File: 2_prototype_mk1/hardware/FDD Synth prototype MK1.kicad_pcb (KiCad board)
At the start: 2 copper layers, 90.2 x 59.7 mm, 21 parts, among them J1 Micro_SD_Card, J2 Conn_02x17_Odd_Even, J3 Conn_01x04_Pin, J4 Conn_01x04_Pin, U1 74AHCT245, U5 MAX98357A

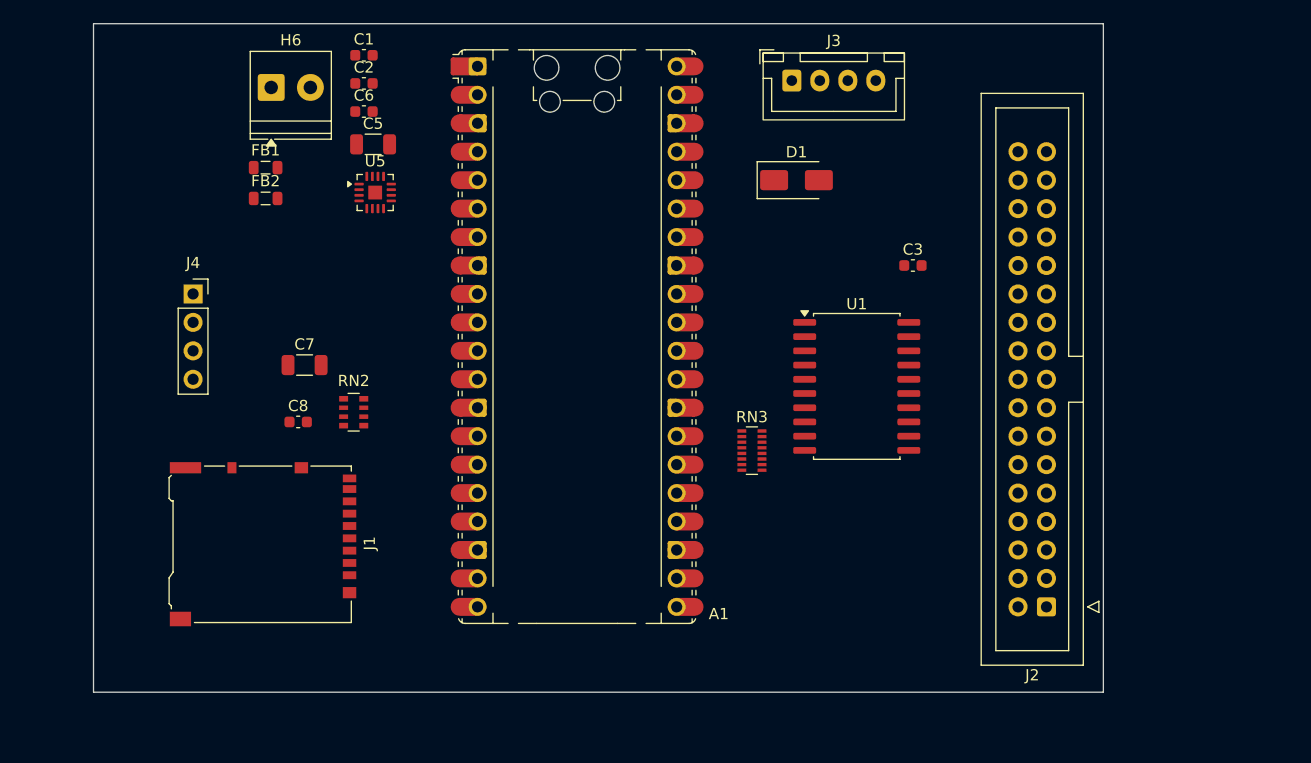
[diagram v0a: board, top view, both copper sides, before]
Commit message: Add OLED screen header
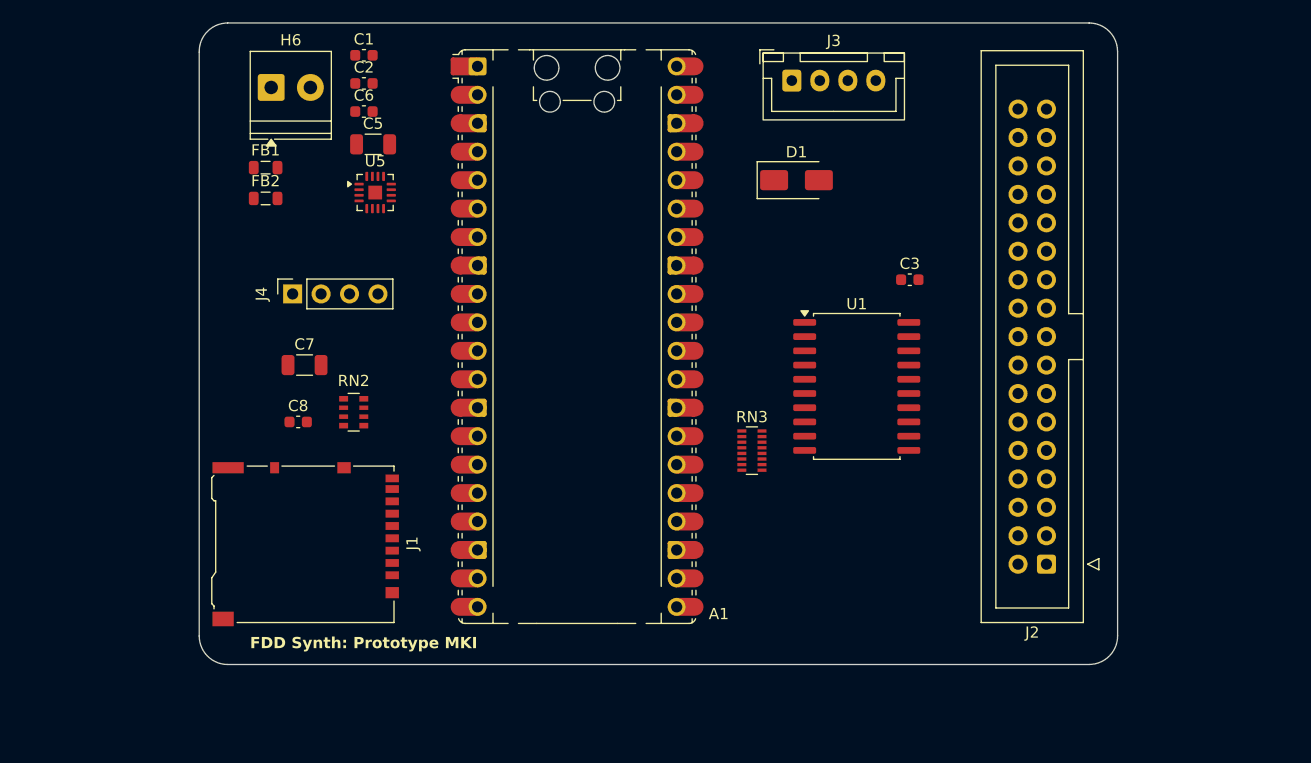
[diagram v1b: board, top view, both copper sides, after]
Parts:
- moved G*** 23.2 mm to (152.4, 96.0), turned to 90 degrees
- moved J4 8.89 mm to (102.9, 94.0), turned to 90 degrees
- moved J1 3.81 mm to (104.0, 116.3)
- moved J2 3.81 mm to (170.2, 118.1)
- moved C3 1.30 mm to (158.0, 92.7)
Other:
- board size 90.2 x 59.7 mm -> 82 x 57.3 mm
- board text added: "FDD Synth: Prototype MKI"

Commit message: Create LED and OLED connections
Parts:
- removed J4: Conn_01x04_Pin, Connector_PinSocket_2.54mm:PinSocket_1x04_P2.54mm_Vertical
- added J5: Conn_01x02, Connector_PinHeader_2.54mm:PinHeader_1x02_P2.54mm_Vertical, F.Cu at (106.7, 92.7)
- added J6: Conn_01x04_Pin, Connector_PinSocket_2.54mm:PinSocket_1x04_P2.54mm_Vertical, F.Cu at (101.6, 101.6)
- added R1: 200R, Resistor_SMD:R_0805_2012Metric, F.Cu at (100.7, 91.4)
- moved RN2 15.3 mm to (114.7, 118.5)
- moved C8 13.1 mm to (114.8, 111.8)
- moved C7 12.0 mm to (114.1, 106.7)
- moved FB2 4.22 mm to (104.3, 83.8)
- moved U1 3.81 mm to (153.2, 98.4)
- moved C3 3.81 mm to (158.0, 88.9)
- moved FB1 1.17 mm to (100.1, 83.8)
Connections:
- A1 pad 5: unconnected-(A1-GPIO3-Pad5)_1 -> /LED/LED_ANODE
- A1 pad 6: unconnected-(A1-GPIO4-Pad6) -> /OLED_I2C_SDA
- A1 pad 7: unconnected-(A1-GPIO5-Pad7) -> /OLED_I2C_SCL
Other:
- board text added: "+"
- board text added: "-"
- board text added: "LED output"
- board text added: "OLED header"

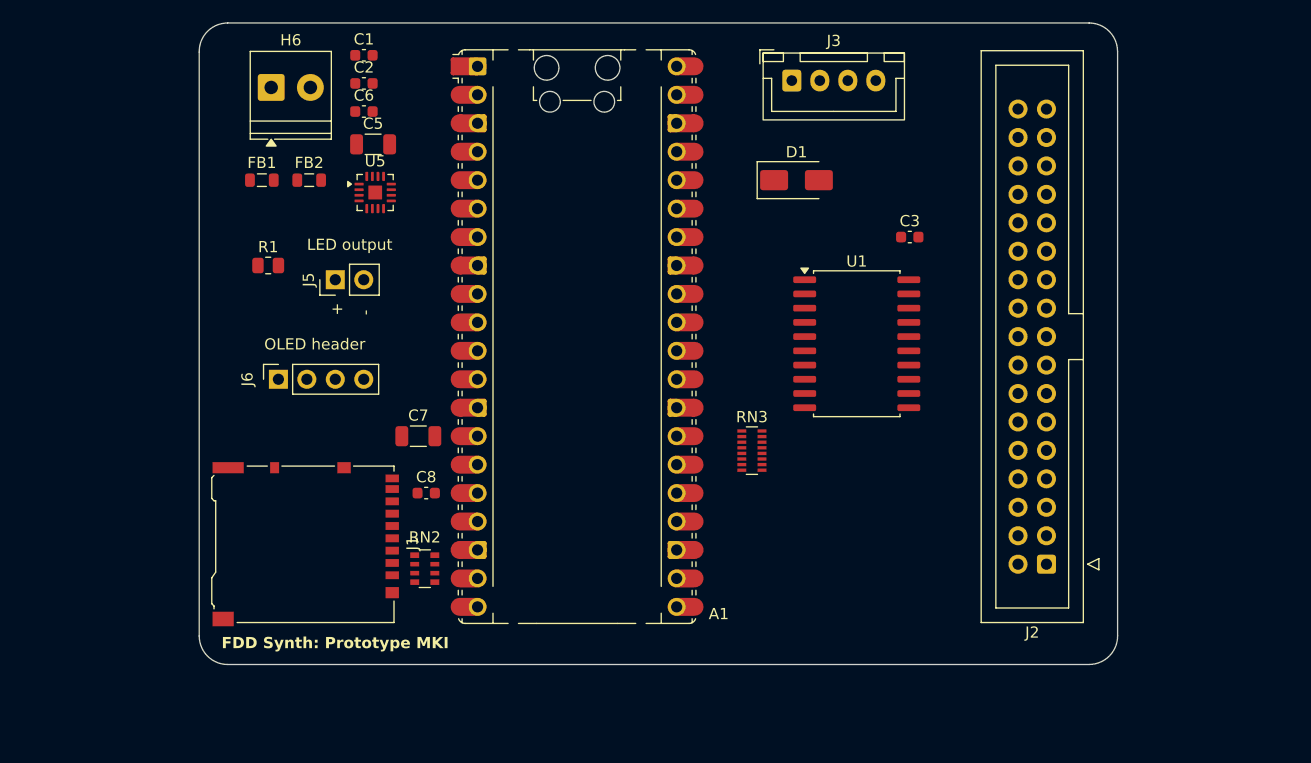
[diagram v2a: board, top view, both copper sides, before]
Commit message: Quick and dirty layout of traces - not final
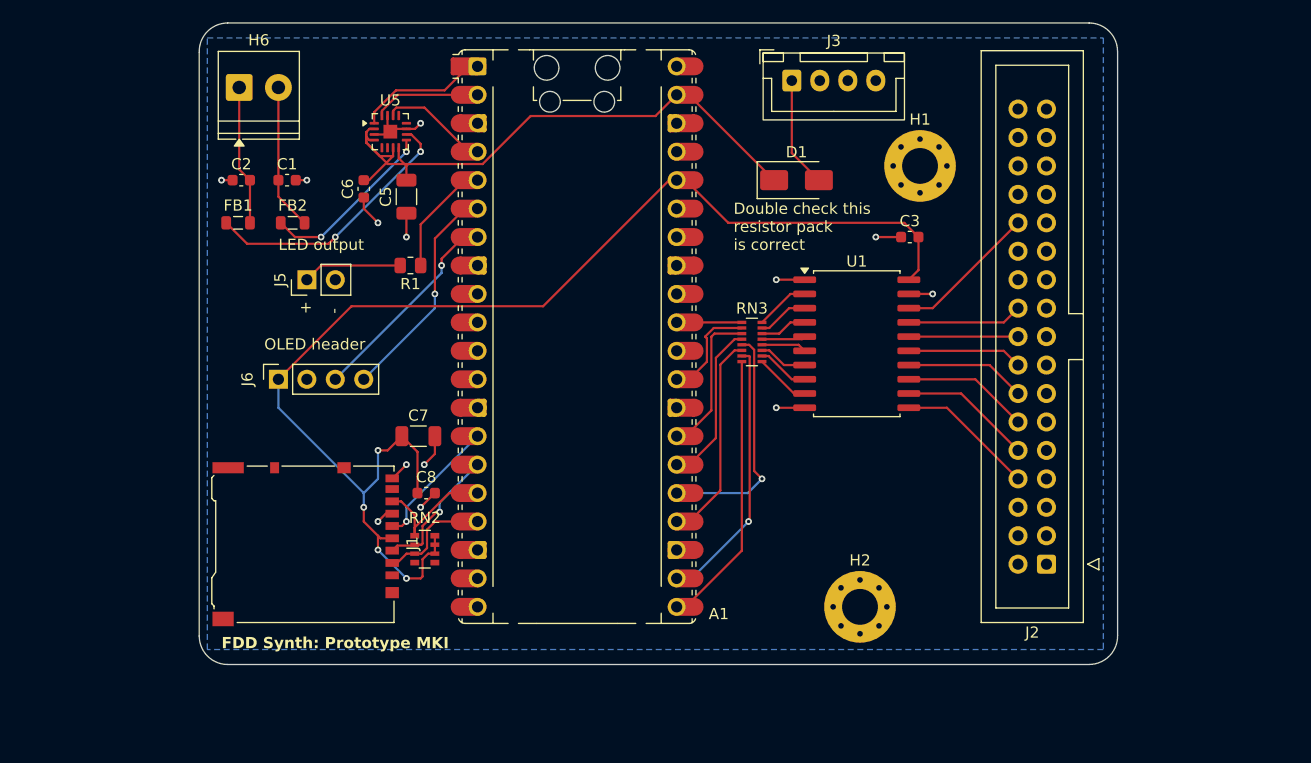
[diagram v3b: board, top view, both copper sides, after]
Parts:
- added H1: MountingHole_Pad, MountingHole:MountingHole_3.2mm_M3_Pad_Via, F.Cu at (158.9, 82.5)
- added H2: MountingHole_Pad, MountingHole:MountingHole_3.2mm_M3_Pad_Via, F.Cu at (153.5, 121.9)
- moved C2 13.9 mm to (98.3, 83.8)
- moved C1 13.1 mm to (102.4, 83.8)
- moved R1 12.7 mm to (113.4, 91.4), turned to 180 degrees
- moved RN3 9.70 mm to (143.9, 98.3)
- moved C6 6.90 mm to (109.2, 84.6), turned to 90 degrees
- moved U5 5.60 mm to (111.6, 79.5)
- moved C5 5.54 mm to (113.0, 85.3), turned to 90 degrees
- moved FB1 4.36 mm to (98.0, 87.6)
- moved FB2 4.09 mm to (102.9, 87.6)
- moved H6 2.86 mm to (98.1, 75.5)
- moved J5 2.54 mm to (104.1, 92.7)
- moved RN2 1.74 mm to (114.7, 116.8)
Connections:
- net Net-(D1-A) renamed +5V
- A1 pad 13: Net-(A1-GND-Pad13) -> GND
- A1 pad 18: Net-(A1-GND-Pad13) -> GND
- A1 pad 23: Net-(A1-GND-Pad13) -> GND
- A1 pad 28: Net-(A1-GND-Pad13) -> GND
- A1 pad 3: Net-(A1-GND-Pad13) -> GND
- A1 pad 33: unconnected-(A1-AGND-Pad33) -> GND
- A1 pad 38: Net-(A1-GND-Pad13) -> GND
- A1 pad 39: Net-(A1-VSYS) -> POWER_5V_SUP
- A1 pad 8: Net-(A1-GND-Pad13) -> GND
- D1 pad 1: Net-(A1-VSYS) -> POWER_5V_SUP
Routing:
- net +3.3V: track 0.00 -> 112.5 mm, vias 0 -> 4
- net POWER_5V_SUP: track 0.00 -> 56.8 mm
- net GND: track 0.00 -> 30.5 mm, vias 0 -> 13
- net /FDD interface/FDD_INDEX: track 0.00 -> 24.8 mm
- net /FDD interface/FDD_MOTOR_A: track 0.00 -> 24.0 mm, vias 0 -> 1
- net Net-(U5-OUTN): track 0.00 -> 23.9 mm, vias 0 -> 2
- net /FDD interface/FDD_DRIVE_SEL_A: track 0.00 -> 21.2 mm, vias 0 -> 1
- net /OLED_I2C_SDA: track 0.00 -> 20.1 mm, vias 0 -> 1
- net /FDD interface/FDD_DRIVE_SEL_B: track 0.00 -> 18.7 mm
- net /OLED_I2C_SCL: track 0.00 -> 18.7 mm, vias 0 -> 1
- net Net-(U5-OUTP): track 0.00 -> 15.9 mm, vias 0 -> 2
- net /FDD interface/FDD_MOTOR_B: track 0.00 -> 14.7 mm
- net /FDD interface/FDD_DIRECTION: track 0.00 -> 13.5 mm
- net Net-(H6-Pin_2): track 0.00 -> 13.1 mm
- net /FDD interface/FDD_CONN_TRACK00: track 0.00 -> 12.9 mm
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- added copper zone on B.Cu, net GND
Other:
- board text added: "Double check this resistor pack is correct"

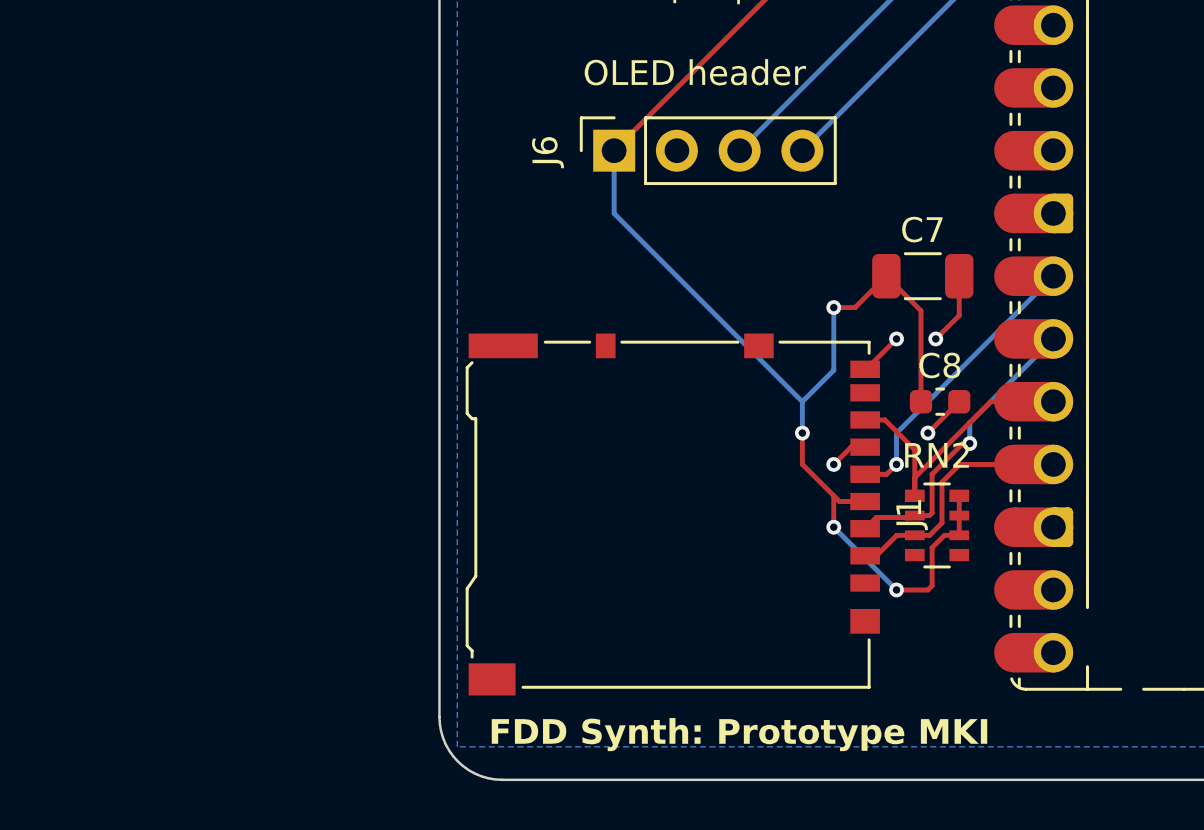
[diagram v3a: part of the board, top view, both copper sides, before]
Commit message: Switch out SD card reader for correct footprint
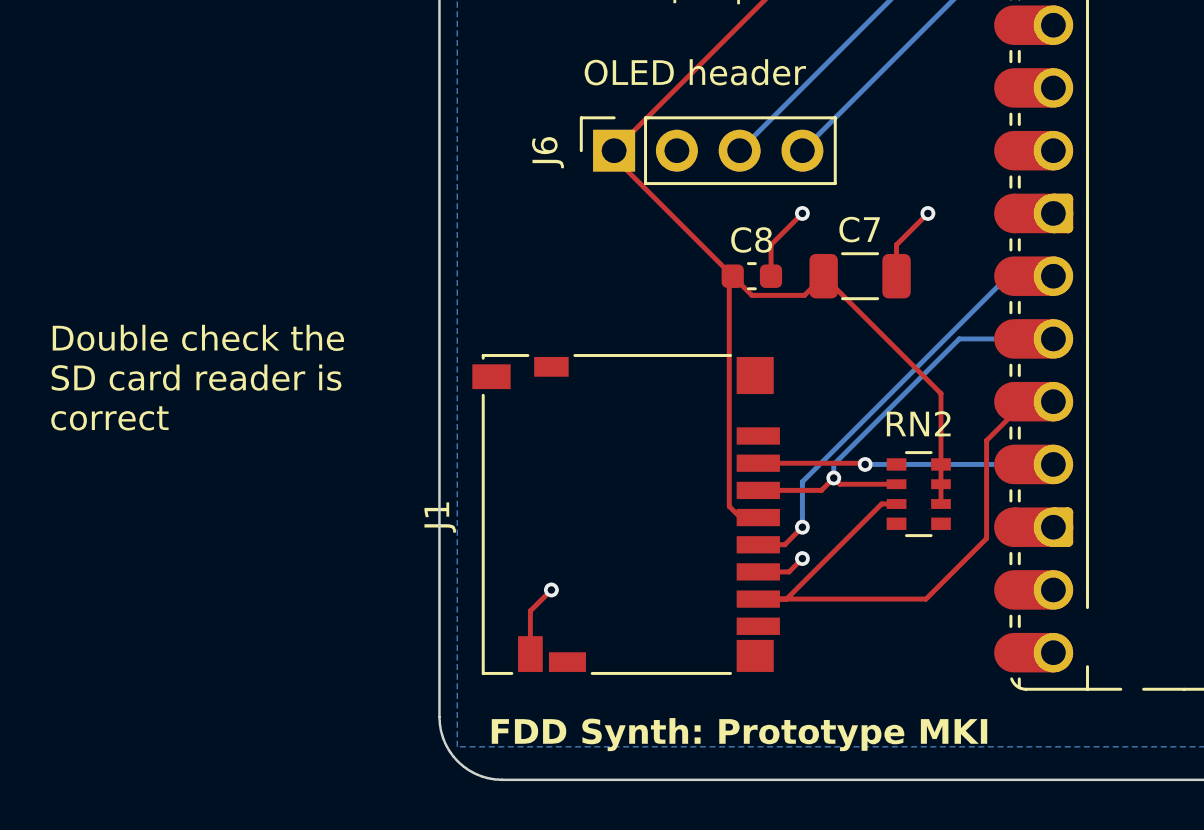
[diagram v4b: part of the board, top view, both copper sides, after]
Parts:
- J1: footprint Connector_Card:microSD_HC_Hirose_DM3AT-SF-PEJM5 -> Connector_Card:microSD_HC_Hirose_DM3D-SF
- moved C8 9.16 mm to (107.2, 106.7)
- moved C7 2.54 mm to (111.6, 106.7)
- moved J1 1.95 mm to (102.1, 116.3), turned to 90 degrees
- moved RN2 1.47 mm to (113.9, 115.5)
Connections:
- RN2 pad 1: /SD card reader/SD_MISO -> /SD card reader/SD_CS
- RN2 pad 3: /SD card reader/SD_CS -> /SD card reader/SD_MISO
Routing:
- net /SD card reader/SD_MISO: track 12.0 -> 24.8 mm
- net +3.3V: track 112.5 -> 103.3 mm, vias 4 -> 0
- net /SD card reader/SD_CLK: track 11.7 -> 17.5 mm
- net /SD card reader/SD_MOSI: track 12.2 -> 17.4 mm
- net GND: track 30.5 -> 33.6 mm
- net /SD card reader/SD_CS: track 10.1 -> 12.0 mm, vias 0 -> 1
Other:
- board text added: "Double check the SD card reader is correct"

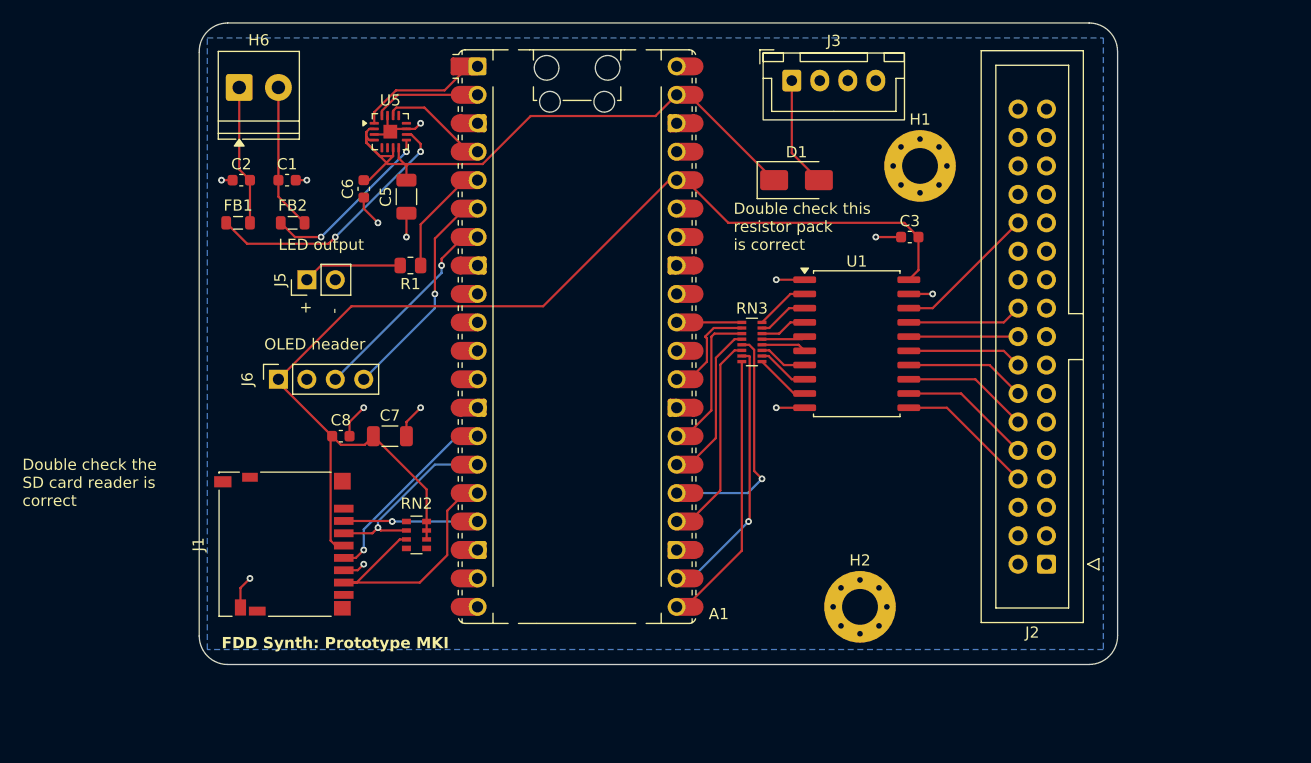
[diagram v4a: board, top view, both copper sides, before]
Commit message: Split power into own schematic
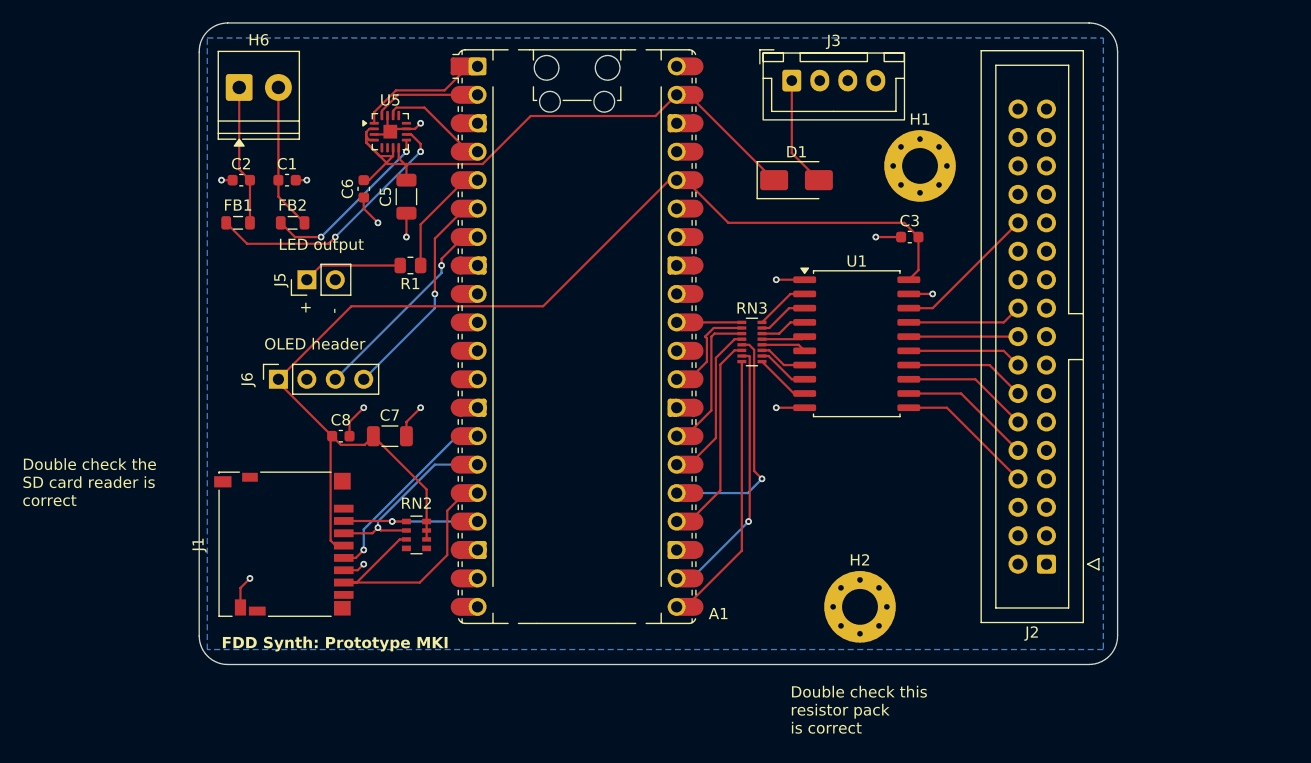
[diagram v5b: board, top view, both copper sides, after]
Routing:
- net /SD card reader/SD_CS: track 12.0 -> 13.2 mm
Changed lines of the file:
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@@
 	)
 	(gr_text "Double check this \nresistor pack \nis correct"
-		(at 142.24 90.17 0)
+		(at 147.32 133.35 0)
 		(layer "F.SilkS")
 		(effects
@@
 		(width 0.2)
 		(layer "F.Cu")
+		(net "/SD card reader/SD_CS")
+	)
+	(segment
+		(start 111.76 114.3)
+		(end 113.03 114.3)
+		(width 0.2)
+		(layer "F.Cu")
